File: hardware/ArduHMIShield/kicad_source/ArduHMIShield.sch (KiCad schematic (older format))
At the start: 29 parts, among them CN1 ARDUINO, Q1 Q_NMOS_GSD, SW1 TAST_HOR, SW2 TAST_HOR, SW3 TAST_HOR, SW4 TAST_HOR, SW5 TAST_HOR, SW6 TAST_HOR

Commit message: reworked schematic and layout, both seem to be finished
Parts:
- added C10, C11, C12, C13, C14: C_0603, capacitors:C_0603, symbol ArduHMIShield-rescue:C_0603
- added IC1, IC2, IC3: SN74LVC2G34, SOT_TO:SOT-23-6, symbol IC_logic:SN74LVC2G34
- added R10, R11, R12, R13, R14, R15, R16, R17, R18, R19, R20: 1k, resistors:R_0603, symbol ArduHMIShield-rescue:R_1206
- added U1: LT1117, SOT_TO:SOT-223, symbol voltage-regulators:LT1117
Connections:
- net labels added: ARDU_A0, ARDU_CLK, ARDU_CLK_1, ARDU_CLK_2, ARDU_CS, ARDU_CS_1, ARDU_CS_2, ARDU_RESET, ARDU_SI, ARDU_SI_1, ARDU_SI_2, BUTTON_DOWN, BUTTON_LEFT, BUTTON_SELECT, BUTTON_UP
- net labels removed: DISPLAY_D4, DISPLAY_D5, DISPLAY_D6, DISPLAY_D7, DISPLAY_E, DISPLAY_RS
- wire segments 202 -> 268
- no-connect marks 21 -> 13
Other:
- note added: "Arduino Uno: SCK=13 MOSI=11\nArduino Leonardo: no spi\nArduino Mega: no spi\nArduino M0 pro: SCK=13 MOSI=11\nArduino Zero: SCK=13 MOSI=11\n\n"
- note removed: "VOUT muss bei 5V an 5V"

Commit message: updated schematic and layout
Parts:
- added D1: green, symbol devices:Led_Small
- added R21: 1k, resistors:R_0603, symbol ArduHMIShield-rescue:R_1206
- C1, C10, C11, C2, C3, C4, C5, C6, C7, C8, C9: value C_0603 -> 1u
- C12, C13, C14: value C_0603 -> 100n
- R10, R11, R12, R13, R14, R15, R16, R17: value 1k -> DNI
- R18, R19, R20: value 1k -> 0R
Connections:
- wire segments 268 -> 276
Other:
- note added: "Copyright generationmake 2018\nsee full project documentation at http://ardutrx.generationmake.de"
- note added: "You may redistribute and modify this documentation under the terms of the CERN OHL v.1.2. (http://ohwr.org/cernohl). \nThis documentation is distributed WITHOUT ANY EXPRESS OR IMPLIED WARRANTY, INCLUDING OF MERCHANTABILITY, SATISFACTORY \nQUALITY AND FITNESS FOR A PARTICULAR PURPOSE. Please see the CERN OHL v.1.2 for applicable conditions"
- note added: "place R10..14 if \nlevel shifter not used"
- note added: "place R15..17 if hardware SPI not possible\nuse software SPI"
- note removed: "Copyright generationmake 2018\nsee full project documentation at http://ardutrx.generationmake.de\n\nThis documentation describes Open Hardware and is licensed \nunder the CERN OHL v. 1.2.\nYou may redistribute and modify this documentation under the terms \nof the CERN OHL v.1.2. (http://ohwr.org/cernohl). This documentation \nis distributed WITHOUT ANY EXPRESS OR IMPLIED WARRANTY, \nINCLUDING O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"
- moved on the sheet: C1, C10, C11, C12, C13, C14, C2, C3, C4, C5, C6, C7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

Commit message: finished layout and generated output files
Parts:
- added U2: TLV733P, SOT_TO:SOT-23-5, symbol voltage-regulators:TLV733P
- D1: footprint (none) -> LEDs:LED_0603
- renumbered IC1 to U3, IC2 to U4, IC3 to U5
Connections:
- wire segments 276 -> 283
- no-connect marks 13 -> 14
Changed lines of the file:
@@
 BUTTON_SELECT
 $Comp
-L IC_logic:SN74LVC2G34 IC3
+L IC_logic:SN74LVC2G34 U5
 U 1 1 5BBD2AFA
 P 3350 7350
-F 0 "IC3" H 3600 7847 60  0000 C CNN
+F 0 "U5" H 3600 7847 60  0000 C CNN
 F 1 "SN74LVC2G34" H 3600 7741 60  0000 C CNN
 F 2 "SOT_TO:SOT-23-6" H 3650 7200 60  0001 C CNN
@@
 $EndComp
 $Comp
-L IC_logic:SN74LVC2G34 IC2
+L IC_logic:SN74LVC2G34 U4
 U 1 1 5BBD2C7D
 P 3350 6800
-F 0 "IC2" H 3600 7297 60  0000 C CNN
+F 0 "U4" H 3600 7297 60  0000 C CNN
 F 1 "SN74LVC2G34" H 3600 7191 60  0000 C CNN
 F 2 "SOT_TO:SOT-23-6" H 3650 6650 60  0001 C CNN
@@
 $EndComp
 $Comp
-L IC_logic:SN74LVC2G34 IC1
+L IC_logic:SN74LVC2G34 U3
 U 1 1 5BBD2CFB
 P 3350 6250
-F 0 "IC1" H 3600 6747 60  0000 C CNN
+F 0 "U3" H 3600 6747 60  0000 C CNN
 F 1 "SN74LVC2G34" H 3600 6641 60  0000 C CNN
 F 2 "SOT_TO:SOT-23-6" H 3650 6100 60  0001 C CNN
@@
 F 0 "D1" V 3146 3582 50  0000 R CNN
 F 1 "green" V 3055 3582 50  0000 R CNN
-F 2 "" V 3100 3650 50  0000 C CNN
+F 2 "LEDs:LED_0603" V 3100 3650 50  0001 C CNN
 F 3 "" V 3100 3650 50  0000 C CNN
 	1    3100 3650
@@
 Text Notes 7000 6900 0    43   ~ 0
 You may redistribute and modify this documentation under the terms of the CERN OHL v.1.2. (http://ohwr.org/cernohl). \nThis documentation is distributed WITHOUT ANY EXPRESS OR IMPLIED WARRANTY, INCLUDING OF MERCHANTABILITY, SATISFACTORY \nQUALITY AND FITNESS FOR A PARTICULAR PURPOSE. Please see the CERN OHL v.1.2  for applicable conditions
+$Comp
+L voltage-regulators:TLV733P U2
+U 1 1 5BBBF98F
+P 1700 4250
+F 0 "U2" H 1700 4637 60  0000 C CNN
+F 1 "TLV733P" H 1700 4531 60  0000 C CNN
+F 2 "SOT_TO:SOT-23-5" H 1700 4400 60  0001 C CNN
+F 3 "" H 1700 4250 60  0000 C CNN
+	1    1700 4250
+	1    0    0    -1
+$EndComp
+$Comp
+L ArduHMIShield-rescue:GND #PWR032
+U 1 1 5BBBFB31
+P 1000 4500
+F 0 "#PWR032" H 1000 4250 50  0001 C CNN
+F 1 "GND" H 1000 4350 50  0000 C CNN
+F 2 "" H 1000 4500 50  0000 C CNN
+F 3 "" H 1000 4500 50  0000 C CNN
+	1    1000 4500
+	1    0    0    -1
+$EndComp
+$Comp
+L ArduHMIShield-rescue:+5V #PWR031
+U 1 1 5BBBFBA4
+P 950 4150
+F 0 "#PWR031" H 950 4000 50  0001 C CNN
+F 1 "+5V" H 950 4290 50  0000 C CNN
+F 2 "" H 950 4150 50  0000 C CNN
+F 3 "" H 950 4150 50  0000 C CNN
+	1    950  4150
+	0    -1   -1   0
+$EndComp
+$Comp
+L power-supply:+3V3 #PWR033
+U 1 1 5BBBFCB3
+P 2450 4150
+F 0 "#PWR033" H 2450 4000 50  0001 C CNN
+F 1 "+3V3" V 2465 4278 50  0000 L CNN
+F 2 "" H 2450 4150 50  0000 C CNN
+F 3 "" H 2450 4150 50  0000 C CNN
+	1    2450 4150
+	0    1    1    0
+$EndComp
+NoConn ~ 2350 4300
+Wire Wire Line
+	950  4150 1000 4150
+Wire Wire Line
+	1000 4500 1000 4450
+Wire Wire Line
+	1000 4450 1050 4450
+Wire Wire Line
+	1050 4300 1000 4300
+Wire Wire Line
+	1000 4300 1000 4150
+Connection ~ 1000 4150
+Wire Wire Line
+	1000 4150 1050 4150
+Wire Wire Line
+	2350 4150 2450 4150
 $EndSCHEMATC

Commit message: updated pcb and schematic to version 1.1, see changes in CHANGES.txt
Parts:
- removed C13, C14: 100n, capacitors:C_0603, symbol ArduHMIShield-rescue:C_0603
- removed SW1, SW2, SW3, SW4, SW5, SW6: TAST_HOR, mechanical-switches:PCB_PUSH, symbol ArduHMIShield-rescue:TAST_HOR
- removed U2: TLV733P, SOT_TO:SOT-23-5, symbol voltage-regulators:TLV733P
- removed U3, U4, U5: SN74LVC2G34, SOT_TO:SOT-23-6, symbol IC_logic:SN74LVC2G34
- added SW1, SW2, SW3, SW4, SW5, SW6: TAST_VER, mechanical-switches:WE_430182050816, symbol mechanical-switches:TAST_VER
- added U2: 74VHC245D, SOIC:SOIC-20_7.5x12.8mm_Pitch1.27mm, symbol IC_logic:74xx245
- Q1: value Q_NMOS_GSD -> 2N7002
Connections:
- wire segments 283 -> 276
- no-connect marks 14 -> 15
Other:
- note added: "Copyright generationmake 2019\nsee full project documentation at http://arduhmi.generationmake.de"
- note removed: "Copyright generationmake 2018\nsee full project documentation at http://ardutrx.generationmake.de"
- moved on the sheet: C12

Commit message: updated design files to better support Aisler
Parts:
- C1, C10, C11, C2, C3, C4, C5, C6, C7, C8, C9: value 1u -> 1uF
- C12: value 100n -> 100nF
- R16: value DNI -> 0R
- R19: value 0R -> DNI
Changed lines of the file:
@@
 P 8100 3200
 F 0 "C7" H 8110 3270 50  0000 L CNN
-F 1 "1u" H 8110 3120 50  0000 L CNN
+F 1 "1uF" H 8110 3120 50  0000 L CNN
 F 2 "capacitors:C_0603" H 8100 3050 50  0001 C CNN
 F 3 "" H 8100 3200 50  0000 C CNN
@@
 P 8100 3500
 F 0 "C8" H 8110 3570 50  0000 L CNN
-F 1 "1u" H 8110 3420 50  0000 L CNN
+F 1 "1uF" H 8110 3420 50  0000 L CNN
 F 2 "capacitors:C_0603" H 8100 3350 50  0001 C CNN
 F 3 "" H 8100 3500 50  0000 C CNN
@@
 P 8100 3900
 F 0 "C9" H 8110 3970 50  0000 L CNN
-F 1 "1u" H 8110 3820 50  0000 L CNN
+F 1 "1uF" H 8110 3820 50  0000 L CNN
 F 2 "capacitors:C_0603" H 8100 3750 50  0001 C CNN
 F 3 "" H 8100 3900 50  0000 C CNN
@@
 P 4700 4450
 F 0 "C6" H 4710 4520 50  0000 L CNN
-F 1 "1u" H 4710 4370 50  0000 L CNN
+F 1 "1uF" H 4710 4370 50  0000 L CNN
 F 2 "capacitors:C_0603" H 4700 4300 50  0001 C CNN
 F 3 "" H 4700 4450 50  0000 C CNN
@@
 P 4400 4450
 F 0 "C4" H 4410 4520 50  0000 L CNN
-F 1 "1u" H 4410 4370 50  0000 L CNN
+F 1 "1uF" H 4410 4370 50  0000 L CNN
 F 2 "capacitors:C_0603" H 4400 4300 50  0001 C CNN
 F 3 "" H 4400 4450 50  0000 C CNN
@@
 P 4100 4450
 F 0 "C3" H 4110 4520 50  0000 L CNN
-F 1 "1u" H 4110 4370 50  0000 L CNN
+F 1 "1uF" H 4110 4370 50  0000 L CNN
 F 2 "capacitors:C_0603" H 4100 4300 50  0001 C CNN
 F 3 "" H 4100 4450 50  0000 C CNN
@@
 P 3800 4450
 F 0 "C2" H 3810 4520 50  0000 L CNN
-F 1 "1u" H 3810 4370 50  0000 L CNN
+F 1 "1uF" H 3810 4370 50  0000 L CNN
 F 2 "capacitors:C_0603" H 3800 4300 50  0001 C CNN
 F 3 "" H 3800 4450 50  0000 C CNN
@@
 P 3500 4450
 F 0 "C1" H 3510 4520 50  0000 L CNN
-F 1 "1u" H 3510 4370 50  0000 L CNN
+F 1 "1uF" H 3510 4370 50  0000 L CNN
 F 2 "capacitors:C_0603" H 3500 4300 50  0001 C CNN
 F 3 "" H 3500 4450 50  0000 C CNN
@@
 P 4400 3500
 F 0 "C5" H 4410 3570 50  0000 L CNN
-F 1 "1u" H 4410 3420 50  0000 L CNN
+F 1 "1uF" H 4410 3420 50  0000 L CNN
 F 2 "capacitors:C_0603" H 4400 3350 50  0001 C CNN
 F 3 "" H 4400 3500 50  0000 C CNN
@@
 P 700 3650
 F 0 "C10" H 710 3720 50  0000 L CNN
-F 1 "1u" H 710 3570 50  0000 L CNN
+F 1 "1uF" H 710 3570 50  0000 L CNN
 F 2 "capacitors:C_0603" H 700 3500 50  0001 C CNN
 F 3 "" H 700 3650 50  0000 C CNN
@@
 P 2600 3650
 F 0 "C11" H 2610 3720 50  0000 L CNN
-F 1 "1u" H 2610 3570 50  0000 L CNN
+F 1 "1uF" H 2610 3570 50  0000 L CNN
 F 2 "capacitors:C_0603" H 2600 3500 50  0001 C CNN
 F 3 "" H 2600 3650 50  0000 C CNN
@@
 P 4200 5600
 F 0 "C12" H 4210 5670 50  0000 L CNN
-F 1 "100n" H 4210 5520 50  0000 L CNN
+F 1 "100nF" H 4210 5520 50  0000 L CNN
 F 2 "capacitors:C_0603" H 4200 5450 50  0001 C CNN
 F 3 "" H 4200 5600 50  0000 C CNN
@@
 P 9500 2750
 F 0 "R16" V 9450 2500 50  0000 L CNN
-F 1 "DNI" V 9550 2850 50  0000 L CNN
+F 1 "0R" V 9550 2850 50  0000 L CNN
 F 2 "resistors:R_0603" H 9500 2600 50  0001 C CNN
 F 3 "" H 9500 2750 50  0000 C CNN
@@
 P 9500 2050
 F 0 "R19" V 9450 1800 50  0000 L CNN
-F 1 "0R" V 9550 2150 50  0000 L CNN
+F 1 "DNI" V 9550 2150 50  0000 L CNN
 F 2 "resistors:R_0603" H 9500 1900 50  0001 C CNN
 F 3 "" H 9500 2050 50  0000 C CNN

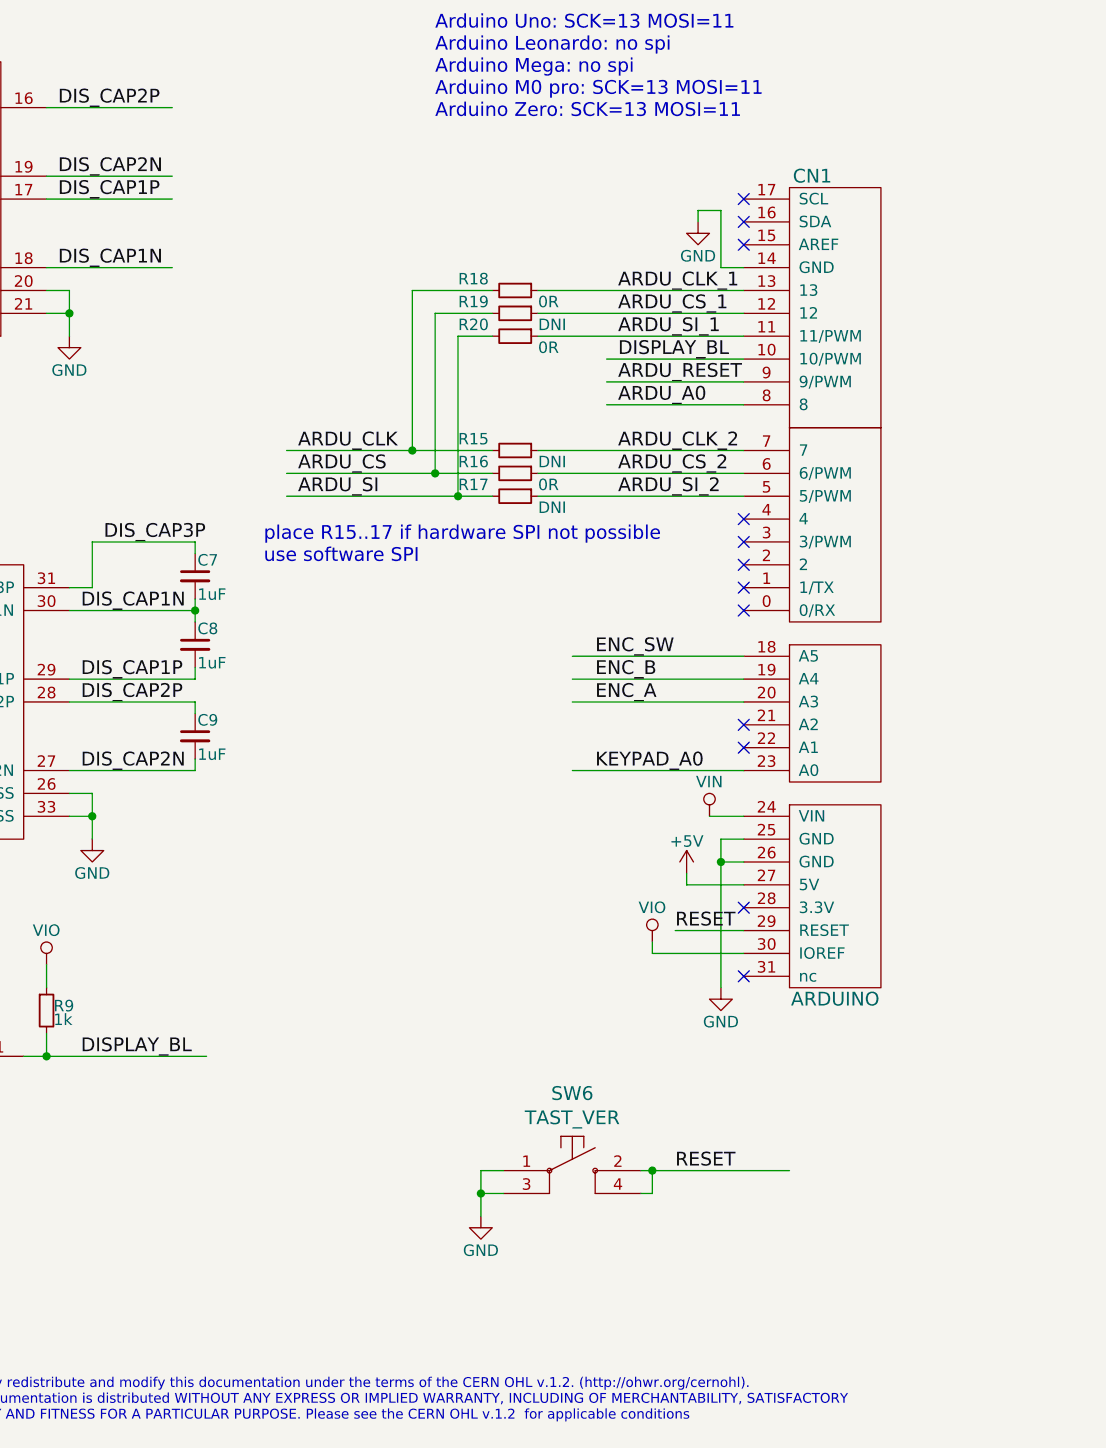
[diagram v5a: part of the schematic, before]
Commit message: added Arduino SPI header, updated all files
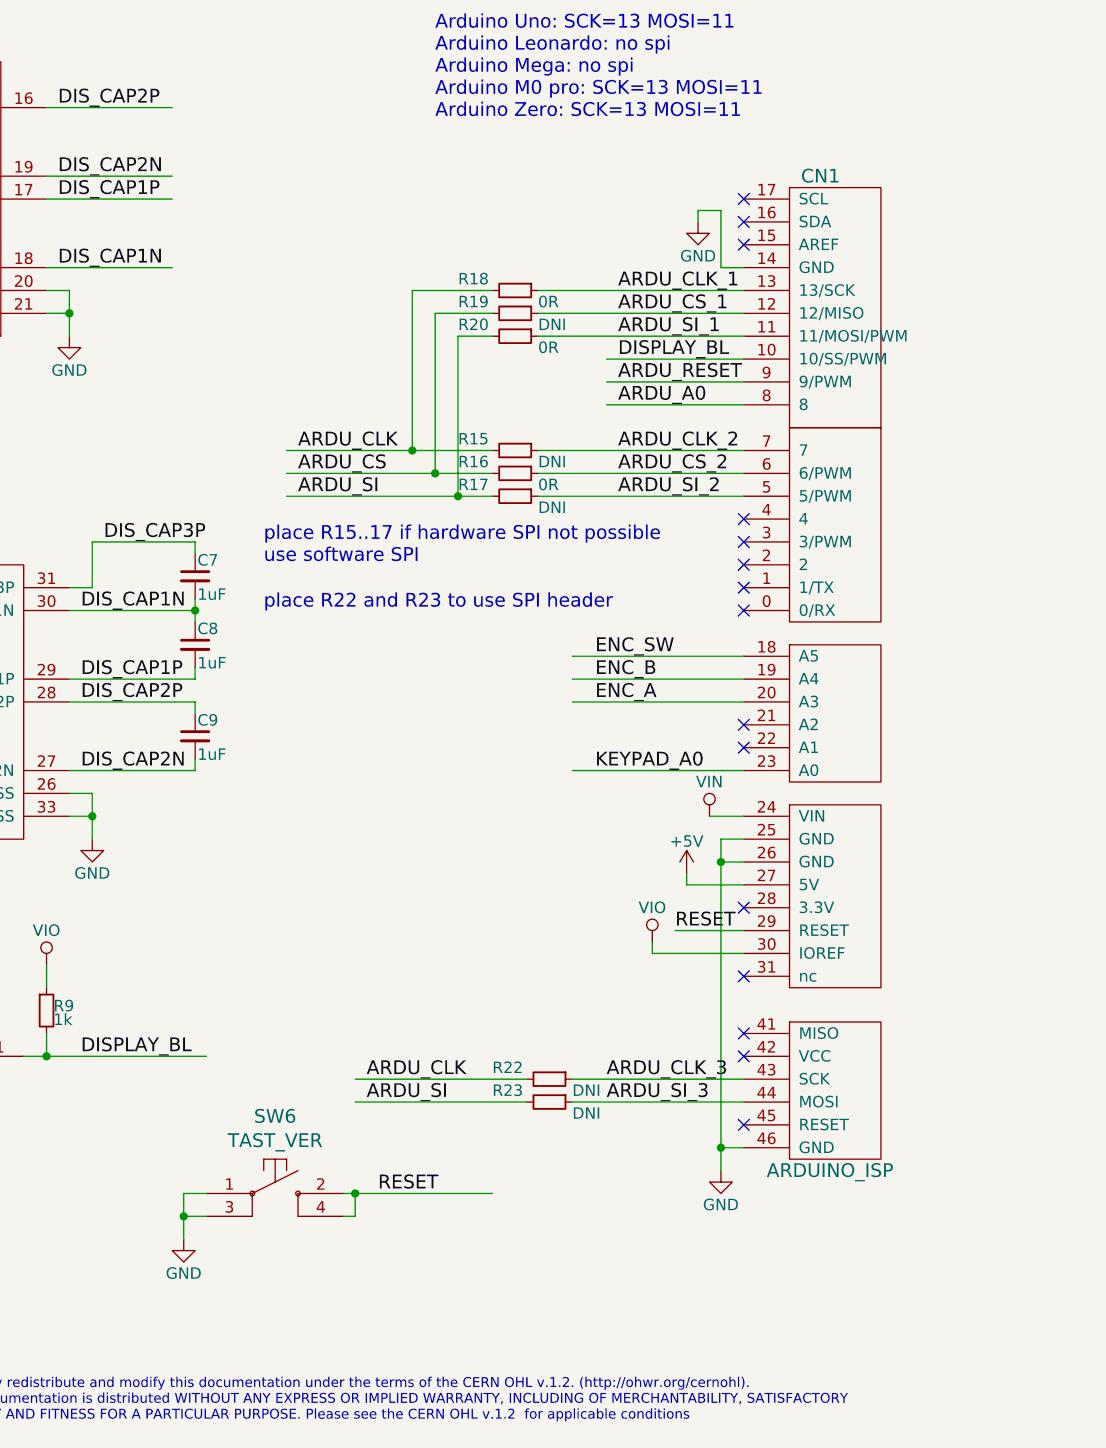
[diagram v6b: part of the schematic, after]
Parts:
- removed CN1: ARDUINO, MODULE_compute:ARDUINO, symbol ArduHMIShield-rescue:ARDUINO
- added CN1: ARDUINO_ISP, MODULE_compute:ARDUINO_ISP, symbol MODULE_compute:ARDUINO_ISP
- added R22, R23: DNI, resistors:R_0603, symbol ArduHMIShield-rescue:R_1206
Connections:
- net labels added: ARDU_CLK_3, ARDU_SI_3
- wire segments 276 -> 282
- no-connect marks 15 -> 18
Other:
- note added: "place R22 and R23 to use SPI header"
- moved on the sheet: SW6
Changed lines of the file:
@@
 Sheet 1 1
 Title "ArduHMI Shield"
-Date "2019-06-24"
-Rev "1.1"
+Date "2019-08-23"
+Rev "1.2"
 Comp "generationmake"
 Comment1 ""
@@
 Comment4 "This documentation describes Open Hardware and is licensed under the CERN OHL v. 1.2."
 $EndDescr
-$Comp
-L ArduHMIShield-rescue:ARDUINO CN1
-U 1 1 5B0B2CBD
-P 10700 3200
-F 0 "CN1" H 10800 4950 60  0000 C CNN
-F 1 "ARDUINO" H 10900 1350 60  0000 C CNN
-F 2 "MODULE_compute:ARDUINO" H 11250 4950 60  0001 C CNN
-F 3 "" H 11350 4000 60  0000 C CNN
-	1    10700 3200
-	1    0    0    -1
-$EndComp
 NoConn ~ 10500 1550
 NoConn ~ 10500 1650
@@
 L ArduHMIShield-rescue:GND #PWR028
 U 1 1 5B0B41D5
-P 10400 5000
-F 0 "#PWR028" H 10400 4750 50  0001 C CNN
-F 1 "GND" H 10400 4850 50  0000 C CNN
-F 2 "" H 10400 5000 50  0000 C CNN
-F 3 "" H 10400 5000 50  0000 C CNN
-	1    10400 5000
+P 10400 5800
+F 0 "#PWR028" H 10400 5550 50  0001 C CNN
+F 1 "GND" H 10400 5650 50  0000 C CNN
+F 2 "" H 10400 5800 50  0000 C CNN
+F 3 "" H 10400 5800 50  0000 C CNN
+	1    10400 5800
 	1    0    0    -1
 $EndComp
@@
 L ArduHMIShield-rescue:GND #PWR014
 U 1 1 5B63E57C
-P 9350 6000
-F 0 "#PWR014" H 9350 5750 50  0001 C CNN
-F 1 "GND" H 9350 5850 50  0000 C CNN
-F 2 "" H 9350 6000 50  0000 C CNN
-F 3 "" H 9350 6000 50  0000 C CNN
-	1    9350 6000
+P 8050 6100
+F 0 "#PWR014" H 8050 5850 50  0001 C CNN
+F 1 "GND" H 8050 5950 50  0000 C CNN
+F 2 "" H 8050 6100 50  0000 C CNN
+F 3 "" H 8050 6100 50  0000 C CNN
+	1    8050 6100
 	1    0    0    -1
 $EndComp
@@
 RESET
 Wire Wire Line
-	10700 5800 10100 5800
-Wire Wire Line
-	10050 5900 10100 5900
-Wire Wire Line
-	10100 5900 10100 5800
-Connection ~ 10100 5800
-Wire Wire Line
-	9450 5800 9350 5800
-Wire Wire Line
-	9350 5800 9350 5900
-Wire Wire Line
-	9450 5900 9350 5900
-Connection ~ 9350 5900
-Text Label 10200 5800 0    60   ~ 0
+	9400 5900 8800 5900
+Wire Wire Line
+	8750 6000 8800 6000
+Wire Wire Line
+	8800 6000 8800 5900
+Connection ~ 8800 5900
+Wire Wire Line
+	8150 5900 8050 5900
+Wire Wire Line
+	8050 5900 8050 6000
+Wire Wire Line
+	8150 6000 8050 6000
+Connection ~ 8050 6000
+Text Label 8900 5900 0    60   ~ 0
 RESET
 Wire Wire Line
-	10400 4450 10400 5000
-Wire Wire Line
 	1450 5200 2100 5200
 Wire Wire Line
@@
 	7450 5300 7350 5300
 Wire Wire Line
-	10100 5800 10050 5800
-Wire Wire Line
-	9350 5900 9350 6000
+	8800 5900 8750 5900
+Wire Wire Line
+	8050 6000 8050 6100
 $Comp
 L displays:EA_DOGM128-6 DIS1
@@
 L mechanical-switches:TAST_VER SW6
 U 1 1 5D125154
-P 9750 5800
-F 0 "SW6" H 9750 6137 60  0000 C CNN
-F 1 "TAST_VER" H 9750 6031 60  0000 C CNN
-F 2 "mechanical-switches:WE_430182050816" H 10600 5850 60  0001 C CNN
-F 3 "" H 10600 5850 60  0000 C CNN
-	1    9750 5800
+P 8450 5900
+F 0 "SW6" H 8450 6237 60  0000 C CNN
+F 1 "TAST_VER" H 8450 6131 60  0000 C CNN
+F 2 "mechanical-switches:WE_430182050816" H 9300 5950 60  0001 C CNN
+F 3 "" H 9300 5950 60  0000 C CNN
+	1    8450 5900
 	1    0    0    -1
 $EndComp
@@
 Wire Wire Line
 	4200 5450 4200 5400
+$Comp
+L MODULE_compute:ARDUINO_ISP CN1
+U 1 1 5D60D7FA
+P 10700 3200
+F 0 "CN1" H 10750 4950 60  0000 L CNN
+F 1 "ARDUINO_ISP" H 10600 600 60  0000 L CNN
+F 2 "MODULE_compute:ARDUINO_ISP" H 11250 4950 60  0001 C CNN
+F 3 "" H 11350 4000 60  0000 C CNN
+	1    10700 3200
+	1    0    0    -1
+$EndComp
+$Comp
+L ArduHMIShield-rescue:R_1206 R23
+U 1 1 5D622E19
+P 9650 5500
+F 0 "R23" V 9600 5250 50  0000 L CNN
+F 1 "DNI" V 9700 5600 50  0000 L CNN
+F 2 "resistors:R_0603" H 9650 5350 50  0001 C CNN
+F 3 "" H 9650 5500 50  0000 C CNN
+	1    9650 5500
+	0    1    1    0
+$EndComp
+$Comp
+L ArduHMIShield-rescue:R_1206 R22
+U 1 1 5D62308D
+P 9650 5400
+F 0 "R22" V 9600 5150 50  0000 L CNN
+F 1 "DNI" V 9700 5500 50  0000 L CNN
+F 2 "resistors:R_0603" H 9650 5250 50  0001 C CNN
+F 3 "" H 9650 5400 50  0000 C CNN
+	1    9650 5400
+	0    1    1    0
+$EndComp
+Wire Wire Line
+	9750 5400 10500 5400
+Wire Wire Line
+	10500 5500 9750 5500
+Text Label 8850 5400 0    60   ~ 0
+ARDU_CLK
+Text Label 8850 5500 0    60   ~ 0
+ARDU_SI
+Text Label 9900 5400 0    60   ~ 0
+ARDU_CLK_3
+Text Label 9900 5500 0    60   ~ 0
+ARDU_SI_3
+Wire Wire Line
+	10400 4450 10400 5700
+Wire Wire Line
+	10500 5700 10400 5700
+Connection ~ 10400 5700
+Wire Wire Line
+	10400 5700 10400 5800
+NoConn ~ 10500 5600
+NoConn ~ 10500 5300
+NoConn ~ 10500 5200
+Wire Wire Line
+	8800 5500 9550 5500
+Wire Wire Line
+	8800 5400 9550 5400
+Text Notes 8400 3350 0    60   ~ 0
+place R22 and R23 to use SPI header
 $EndSCHEMATC

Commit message: updated layout to get nicer 3D model
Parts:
- C1, C10, C11, C12, C2, C3, C4, C5, C6, C7, C8, C9: symbol ArduHMIShield-rescue:C_0603 -> ArduHMIShield-rescue:C_0603-ArduHMIShield-rescue
- CN1: footprint MODULE_compute:ARDUINO_ISP -> MODULE_compute:ARDUINO_ISP_TOP
- Q1: symbol ArduHMIShield-rescue:Q_NMOS_GSD -> ArduHMIShield-rescue:Q_NMOS_GSD-ArduHMIShield-rescue
- R1, R10, R11, R12, R13, R14, R15, R16, R17, R18, R19, R2, R20, R21, R22, R23, R3, R4, R5, R6, R7, R8, R9: symbol ArduHMIShield-rescue:R_1206 -> ArduHMIShield-rescue:R_1206-ArduHMIShield-rescue
- SW1, SW2, SW3, SW4, SW5: footprint mechanical-switches:WE_430182050816 -> mechanical-switches:WE_430182080816
